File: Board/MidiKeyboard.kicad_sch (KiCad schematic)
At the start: 34 parts, among them J1 USB_C_Receptacle_16P, J2 Bat, Q1 DMP3099L, SW1 CK_KMS2xxG, SW66 RESET, U1 ESP32-C3, U2 XC6220B331MR, U3 TP4056-42-ESOP8, U4 TCA8418RTWR

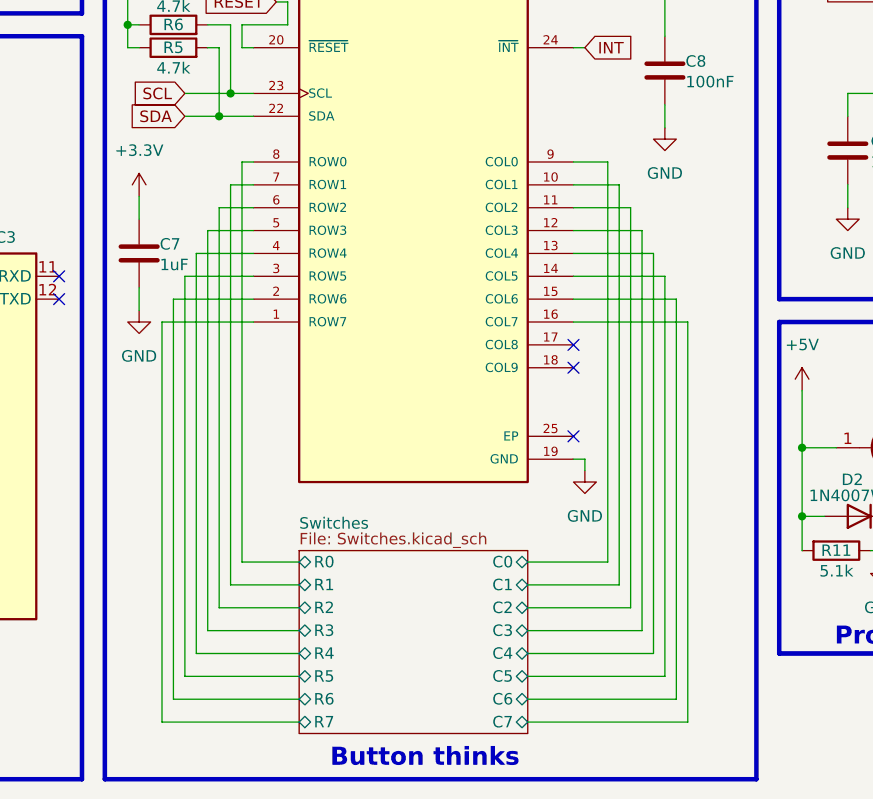
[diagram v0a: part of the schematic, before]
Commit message: Uprava pro jednodusi kontrolu
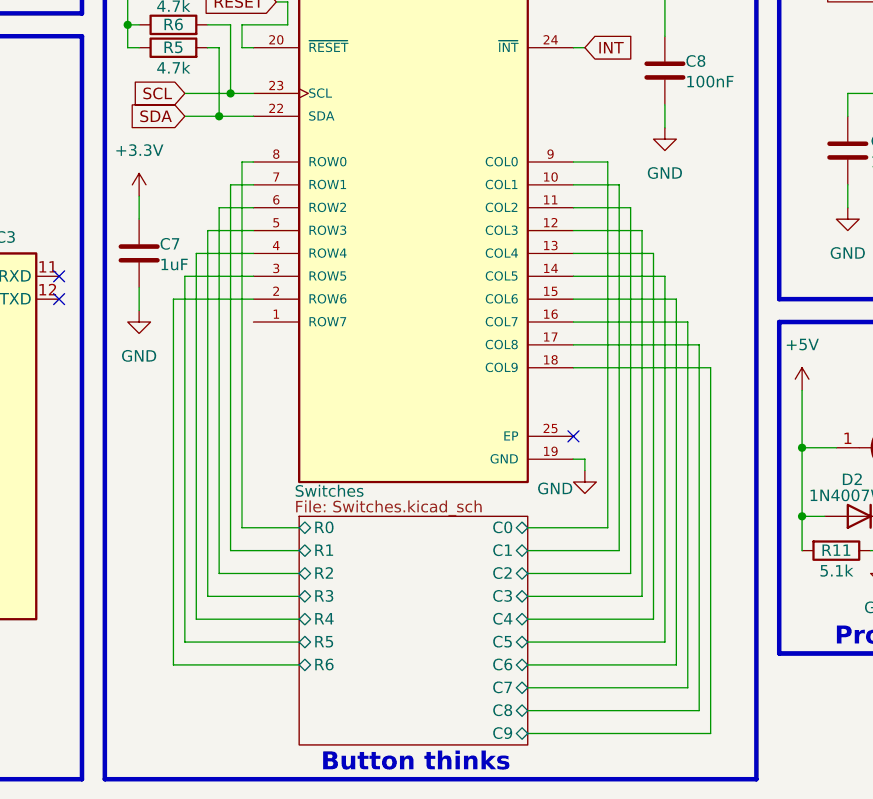
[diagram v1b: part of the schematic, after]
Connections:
- net Switches/C8: now reaches U4.17 (COL8)
- net Switches/C9: now reaches U4.18 (COL9)
- net Switches/R7: no longer names the net of U4.1 (ROW7)
- no-connect marks 11 -> 9
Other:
- sheet Switches ports: added C8, C9; removed R7
